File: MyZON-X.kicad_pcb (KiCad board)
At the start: 2 copper layers, 29 parts, among them J1 Connector ZX81, J2 Audio, SW1 SW_DIP_x03, U1 AY-3-8910, U2.1 74HCT74, U3.1 74HCT08, U4.1 74HCT11, U5.1 74HCT02

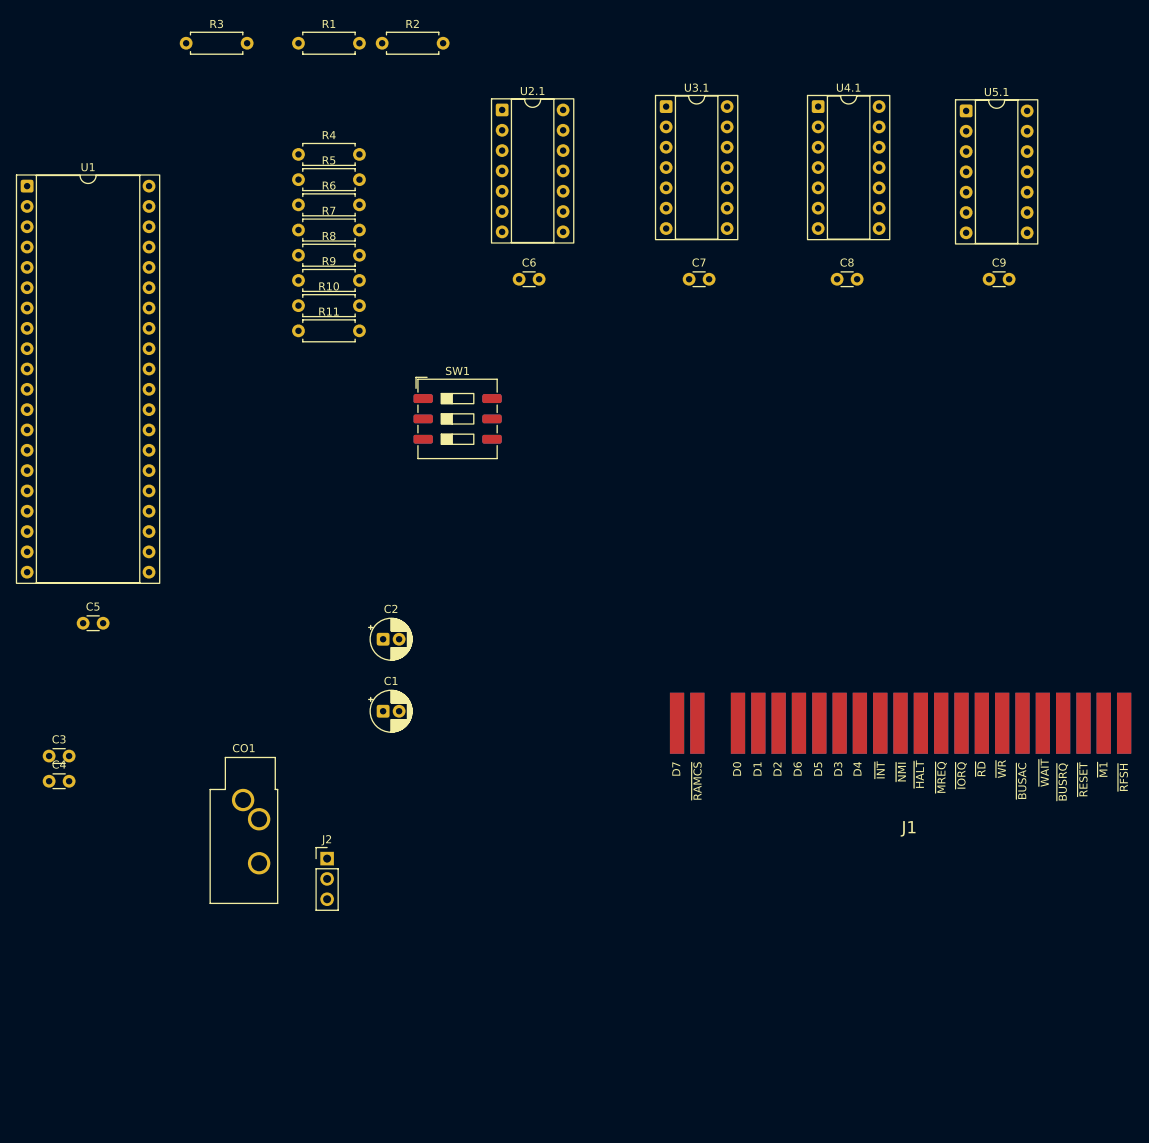
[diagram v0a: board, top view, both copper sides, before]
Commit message: Added Auto Jack Added Board outline Layed out some components in Board outline
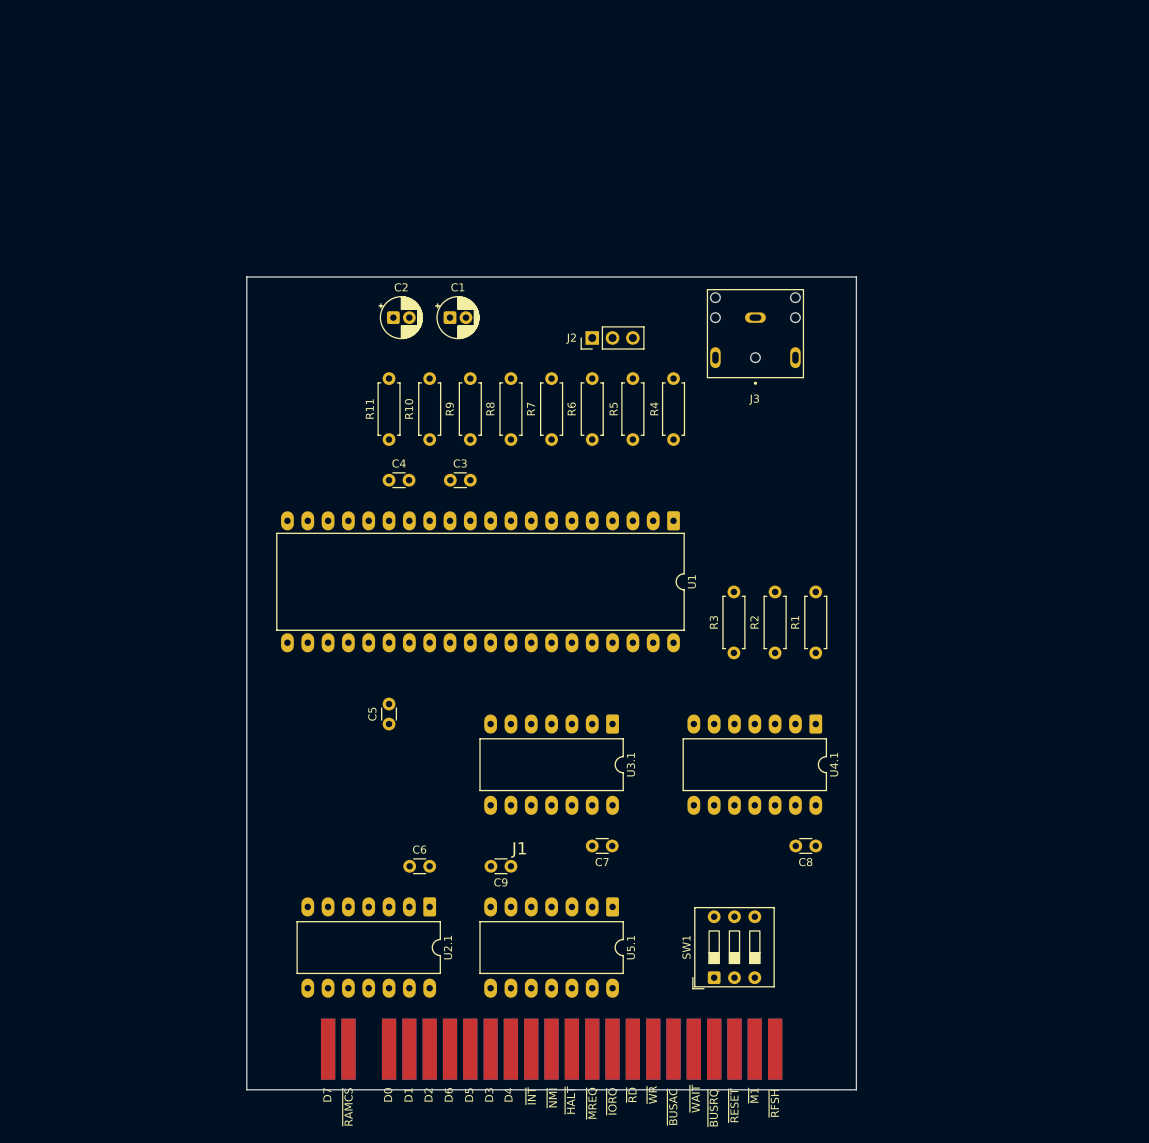
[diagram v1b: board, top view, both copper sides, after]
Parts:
- removed CO1: PSG01538, Connector_Audio:Jack_3.5mm_CUI_SJ1-3533NG_Horizontal_CircularHoles
- added J3: SJ1-3523N, AudioJack:CUI_SJ1-3523N, F.Cu at (124.5, 50.8)
- SW1: footprint Button_Switch_SMD:SW_DIP_SPSTx03_Slide_9.78x9.8mm_W8.61mm_P2.54mm -> Button_Switch_THT:SW_DIP_SPSTx03_Slide_9.78x9.8mm_W7.62mm_P2.54mm
- U1: footprint Package_DIP:DIP-40_W15.24mm_Socket -> Package_DIP:DIP-40_W15.24mm_LongPads
- U2.1, U3.1, U4.1, U5.1: footprint Package_DIP:DIP-14_W7.62mm_Socket -> Package_DIP:DIP-14_W10.16mm_LongPads
- moved U5.1 108.9 mm to (106.7, 124.5), turned to -90 degrees
- moved U2.1 100.0 mm to (83.8, 124.5), turned to -90 degrees
- moved R3 96.9 mm to (121.8, 85.1), turned to -90 degrees
- moved C9 94.6 mm to (94.0, 119.4), turned to 180 degrees
- moved R1 94.3 mm to (132.1, 85.1), turned to -90 degrees
- moved U1 91.0 mm to (114.3, 76.2), turned to -90 degrees
- moved R2 84.4 mm to (127.0, 85.1), turned to -90 degrees
- moved U3.1 77.5 mm to (106.7, 101.6), turned to -90 degrees
- moved U4.1 77.2 mm to (132.1, 101.6), turned to -90 degrees
- moved SW1 76.9 mm to (119.4, 133.3), turned to 90 degrees
- moved C6 74.6 mm to (81.3, 119.4)
- moved J2 73.0 mm to (104.1, 53.3), turned to 90 degrees
- moved C7 71.5 mm to (106.6, 116.8), turned to 180 degrees
- moved C8 70.9 mm to (132.1, 116.8), turned to 180 degrees
- moved C3 60.9 mm to (86.4, 71.1)
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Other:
- board outline added: 76.2 x 101.6 mm
